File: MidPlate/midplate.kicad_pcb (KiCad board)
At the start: 2 copper layers, 180 x 150 mm, 73 parts, among them J1 XT60, J12 JST_B4B-XH-A, J13 JST_BM04B-GHS-TBT, J2 XT60, J3 RA1H1C112R, J4 TE_2-1445053-2_2PIN, J5 TE_2-1445053-2_2PIN, J7 1586842-6, J9 JST_BM04B-GHS-TBT, Q1 MCU60P04-TP, Q2 MCU60P04-TP, U1 LM2576

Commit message: midplate v1 ready for review
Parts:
- C18: footprint Capacitor_SMD:C_1206_3216Metric -> bots:C_1206_3216Metric
- D1: footprint bots:D_SMB -> bots:D_SMA
- L1: value CLF10040T-6R8N-D -> SRP1050WA-101M; footprint bots:IND_10040_TDK -> bots:SRP1050WA-101M
- moved L1 0.99 mm to (138.7, 16.6)
- renumbered CR1 to D2
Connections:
- H5 pad 1: unconnected-(H5-Pad1) -> +5V
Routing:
- net GND: track 2.40 -> 0.00 mm
- net +5V: track 19.4 -> 17.5 mm

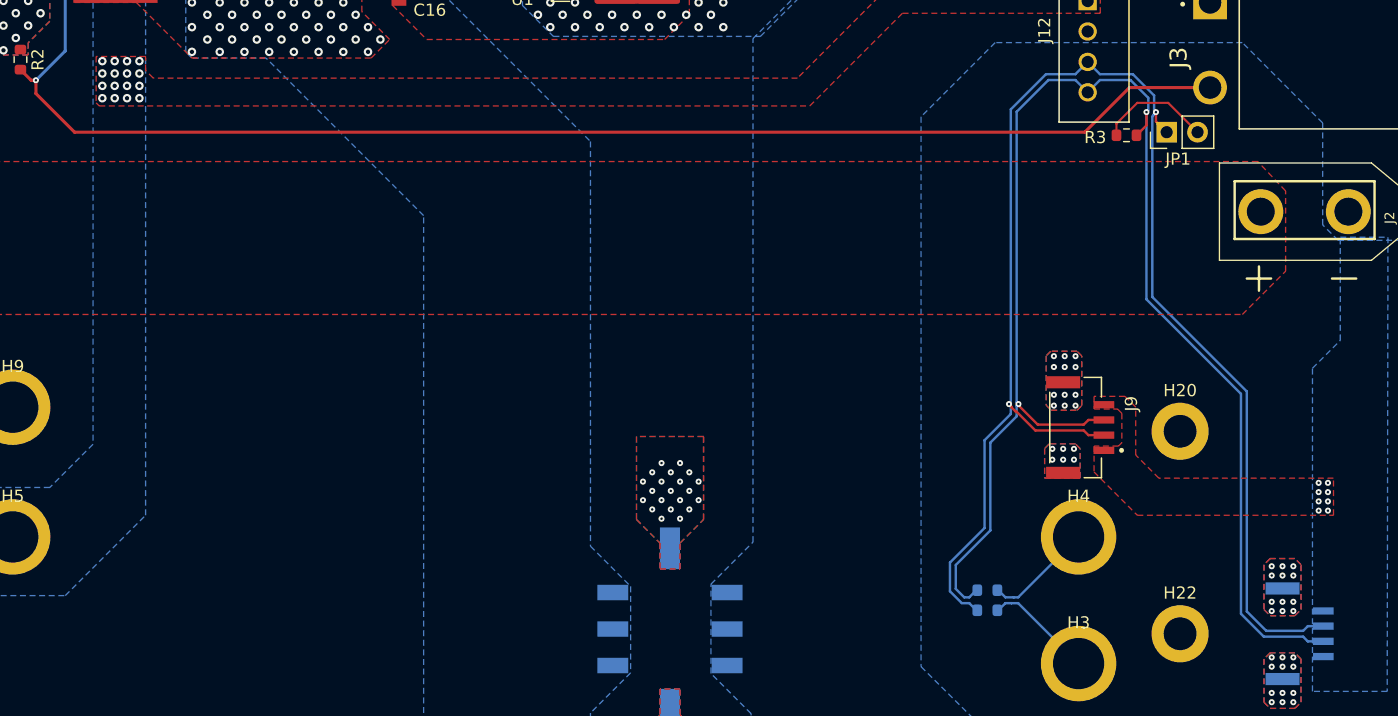
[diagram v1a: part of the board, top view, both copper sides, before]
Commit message: swapped pins around for CAN
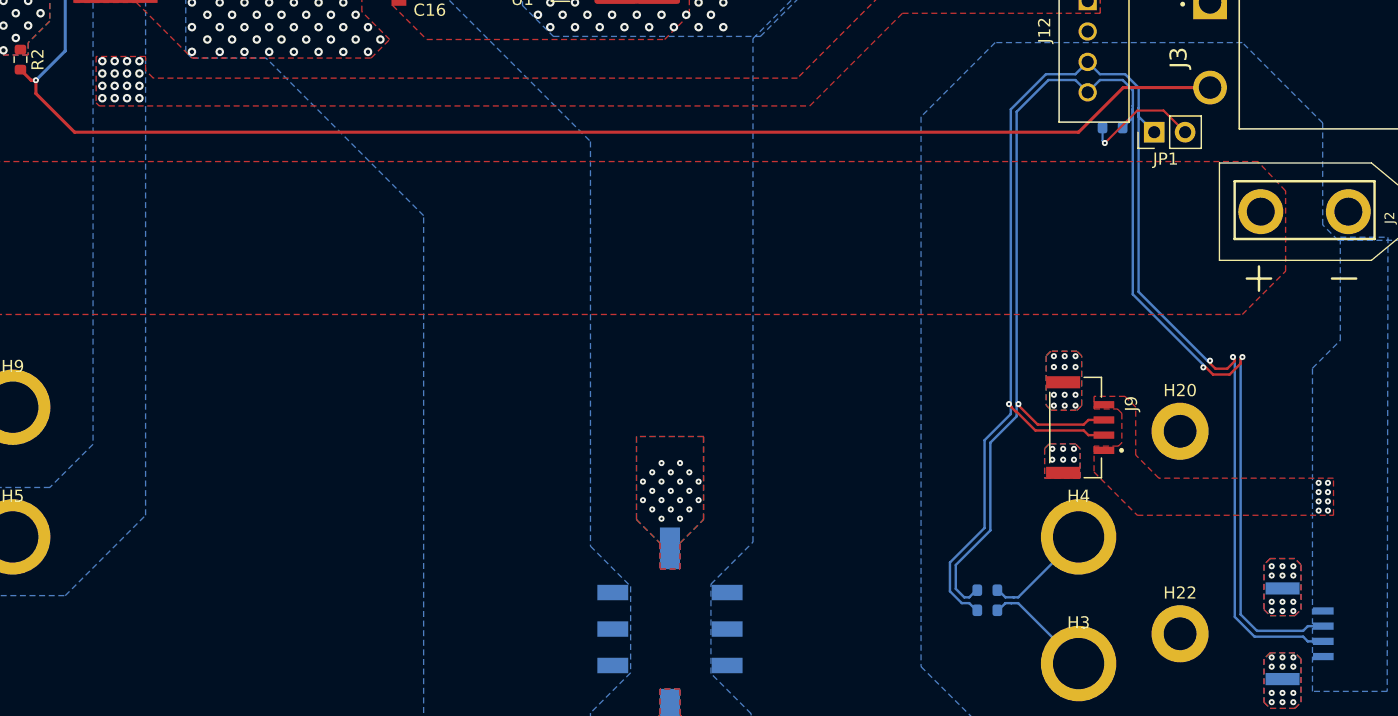
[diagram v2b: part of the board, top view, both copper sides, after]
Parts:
- R3: moved to B.Cu
- moved R3 1.31 mm to (192.0, 42.5)
- moved JP1 1.02 mm to (195.4, 42.9)
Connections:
- J13 pad 2: CAN- -> CAN+
- J13 pad 3: CAN+ -> CAN-
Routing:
- net CAN-: track 123.1 -> 126.8 mm, vias 2 -> 3
- net CAN+: track 120.7 -> 123.6 mm, vias 2 -> 3
- net Net-(JP1-B): track 9.33 -> 9.79 mm, vias 0 -> 1

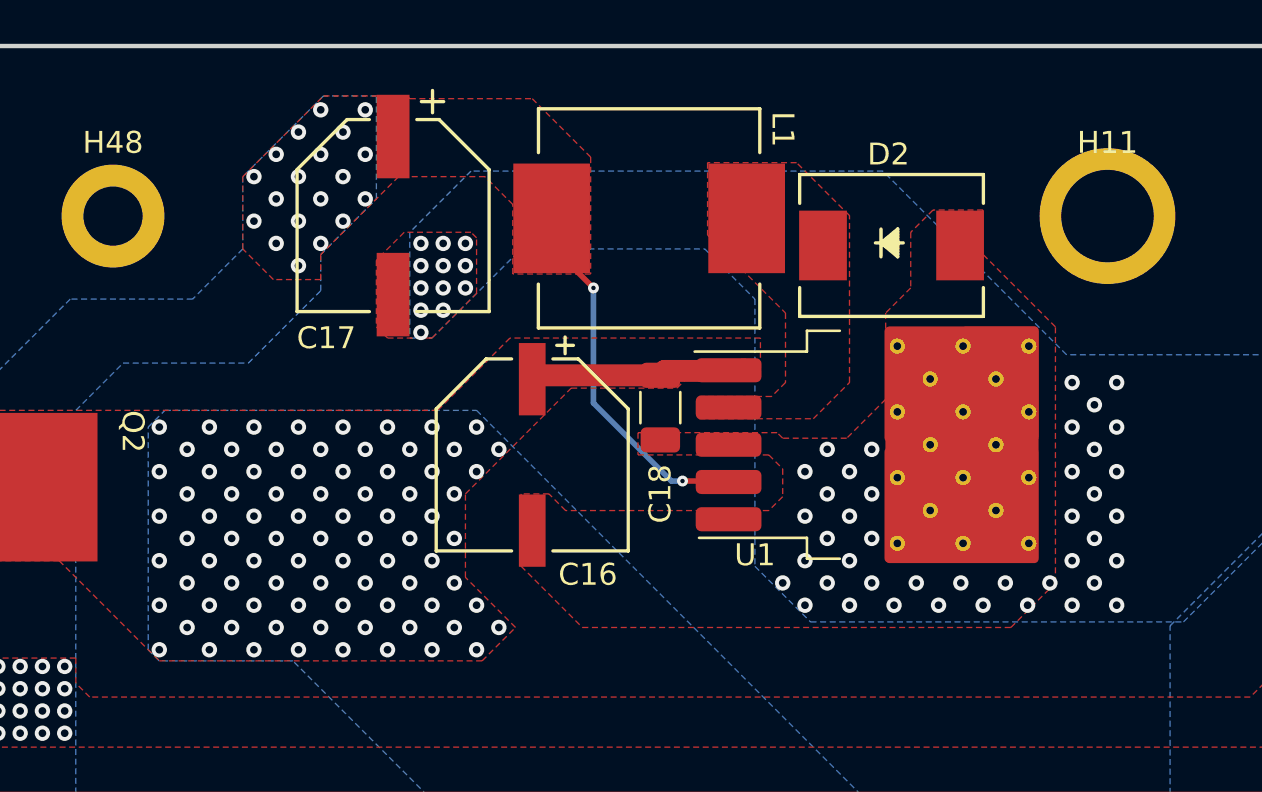
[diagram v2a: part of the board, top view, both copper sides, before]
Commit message: midplate update with different buck regulator pad size
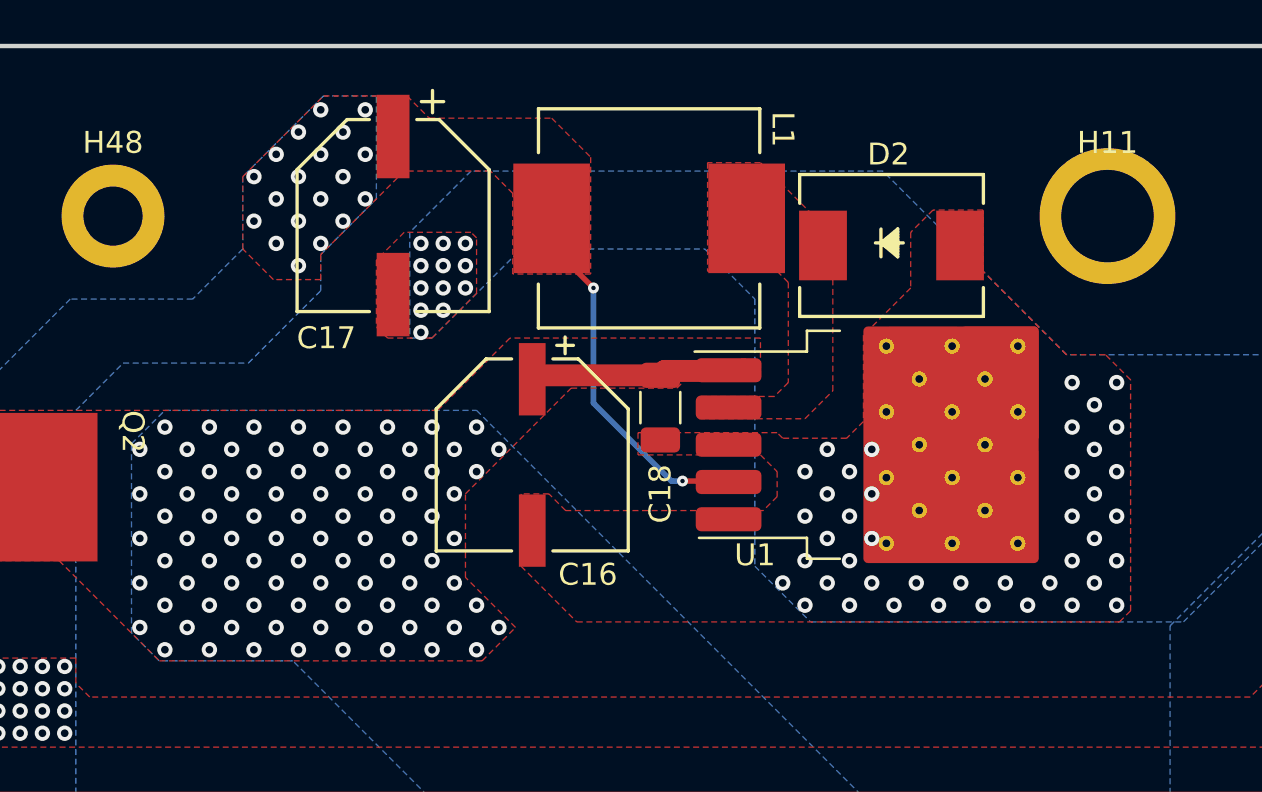
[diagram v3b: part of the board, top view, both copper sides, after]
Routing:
- net VCC: vias 83 -> 88

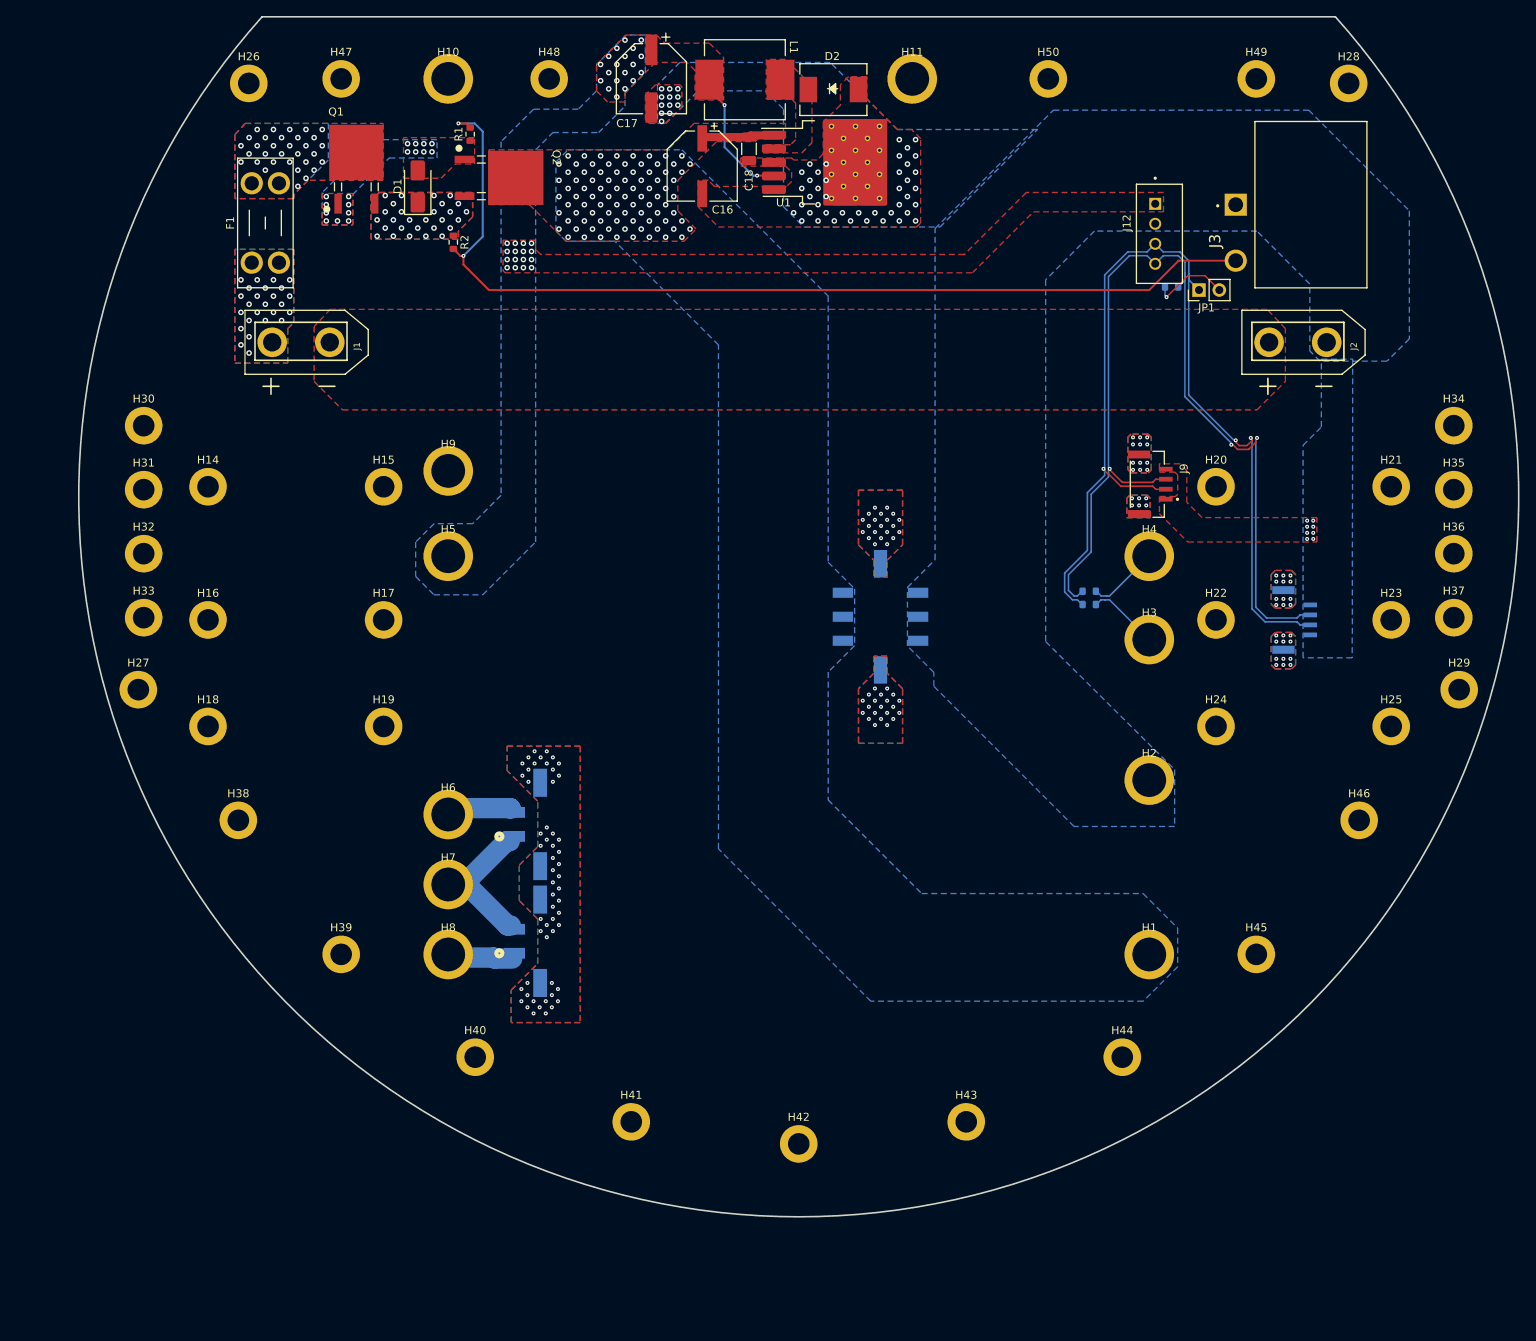
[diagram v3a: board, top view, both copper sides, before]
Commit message: update to midplate and powerboard
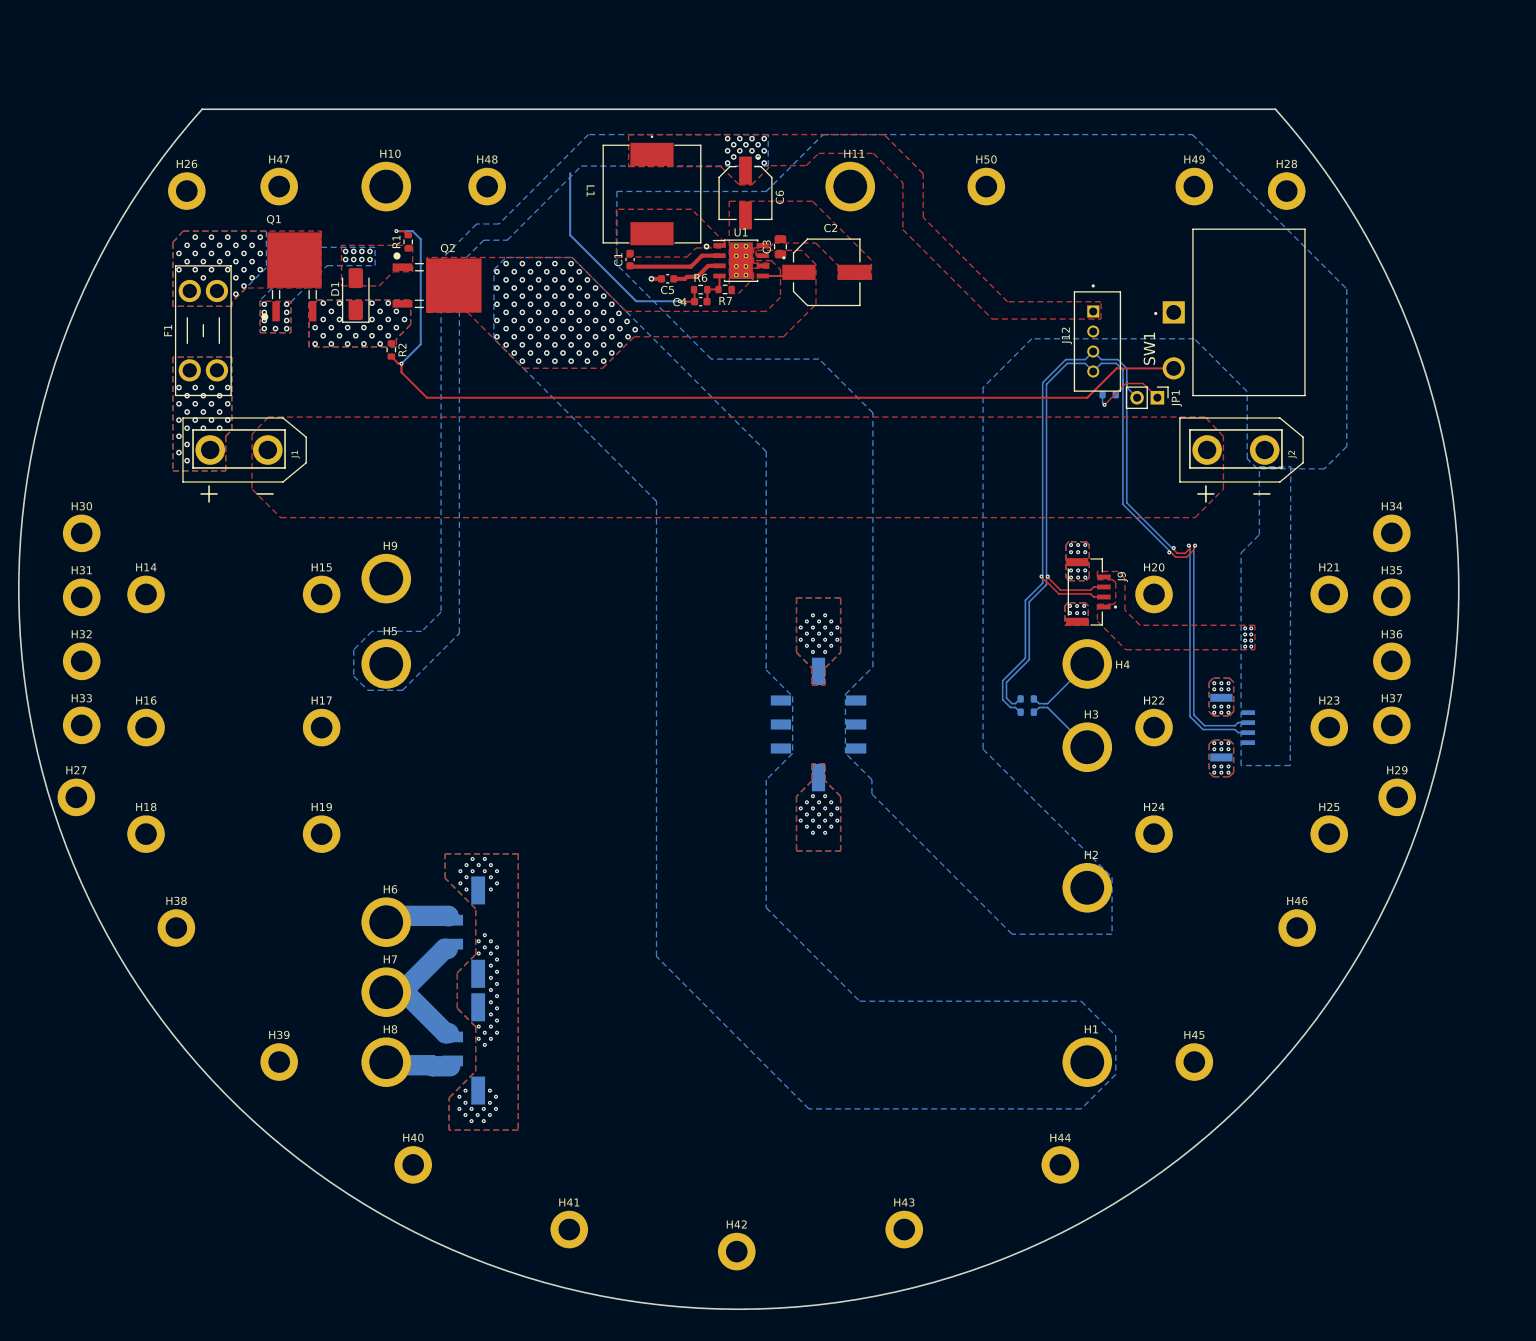
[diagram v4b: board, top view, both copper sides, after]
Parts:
- removed C16: 25SVPF100M, bots:PCAP_SVP_E7_PAN
- removed C17: EEE-1CA471UP, bots:CAP_EEE_F_PAN
- removed C18: 0.47u, bots:C_1206_3216Metric
- removed D2: B540C-13-F, bots:SMC_DIO
- added C1: C_0.1u, bots:C_0603_1608Metric, F.Cu at (124.3, 39.1)
- added C2: 25SVPF100M, bots:CAP_25SVPF100M, F.Cu at (148.9, 40.7)
- added C3: 10u, bots:C_0805_2012Metric, F.Cu at (143.1, 37.5)
- added C4: C_30p, bots:C_0603_1608Metric, F.Cu at (133.2, 44.4)
- added C5: 2.2u, bots:C_0603_1608Metric, F.Cu at (129.0, 41.5)
- added C6: 16SVPF180M, bots:CAP_16SVPF180M, F.Cu at (138.8, 30.8)
- added R6: 88.7k, bots:R_0603_1608Metric, F.Cu at (133.2, 42.9)
- added R7: 22.1k, bots:R_0603_1608Metric, F.Cu at (136.2, 42.9)
- L1: value SRP1050WA-101M -> CDRH127/LDNP-220MC; footprint bots:SRP1050WA-101M -> bots:IND_CDRH127_LDNP-470MC_SUM
- U1: value LM2576 -> LMR23630AFDDAR; footprint bots:TO-263-5_TabPin3_LM2576 -> bots:TI_SO-PowerPAD-8_ThermalVias
- moved L1 18.4 mm to (127.1, 30.9), turned to -90 degrees
- moved U1 17.5 mm to (138.2, 39.3)
- moved R3 15.6 mm to (184.2, 56.0), turned to 180 degrees
- moved J13 15.5 mm to (198.3, 97.6)
- moved J7 15.5 mm to (152.6, 100.2)
- moved J9 15.5 mm to (180.2, 80.7)
- moved H42 15.5 mm to (137.7, 163.1)
- moved H28 15.5 mm to (206.4, 30.6)
- moved H49 15.5 mm to (194.9, 30.0)
- moved H50 15.5 mm to (168.9, 30.0)
- moved F1 15.5 mm to (69.3, 53.0)
- moved H15 15.5 mm to (85.8, 81.0)
- moved H17 15.5 mm to (85.8, 97.6)
- moved H19 15.5 mm to (85.8, 110.9)
- moved H38 15.5 mm to (67.6, 122.7)
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- renumbered J3 to SW1
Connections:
- JP1 pad 1: CAN- -> Net-(JP1-A)
- JP1 pad 2: Net-(JP1-B) -> CAN-
- R3 pad 1: Net-(JP1-B) -> CAN+
- R3 pad 2: CAN+ -> Net-(JP1-A)
- U1 pad 1: VCC -> /Power Input/LM_OUT
- U1 pad 2: /Power Input/LM_OUT -> /Power Input/BOOT
- U1 pad 3: GND -> /Power Input/U1_VCC
- U1 pad 4: +5V -> /Power Input/FB
- U1 pad 5: GND -> VCC
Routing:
- net /Power Input/BOOT: track 0.00 -> 11.8 mm
- net +5V: track 17.5 -> 28.3 mm, vias 37 -> 16
- net Net-(JP1-A): track 0.00 -> 9.82 mm, vias 0 -> 1
- net Net-(JP1-B): track 9.79 -> 0.00 mm, vias 1 -> 0
- net /Power Input/U1_VCC: track 0.00 -> 6.38 mm
- net VCC: track 9.83 -> 4.72 mm, vias 88 -> 95
- net /Power Input/FB: track 0.00 -> 4.68 mm
- net GND: track 0.00 -> 1.26 mm, vias 62 -> 9
- net /Power Input/LM_OUT: track 0.77 -> 0.00 mm
